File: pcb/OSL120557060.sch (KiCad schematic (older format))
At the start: 75 parts, among them J1 USB_B_Micro, J2 USB_B_Micro, J3 AVR-ISP-6, SW1 SW_SPST, SW10 SW_SPST, SW11 SW_SPST, SW12 SW_SPST, SW13 SW_SPST, SW14 SW_SPST, SW15 SW_SPST, SW16 SW_SPST, SW17 SW_SPST, SW18 SW_SPST, SW19 SW_SPST, SW2 SW_SPST, SW20 SW_SPST, SW21 SW_SPST, SW22 SW_SPST, SW23 SW_SPST, SW24 SW_SPST, SW25 SW_SPST, SW26 SW_SPST, SW27 SW_SPST, SW28 SW_SPST, SW29 SW_SPST, SW3 SW_SPST, SW30 SW_SPST, SW4 SW_SPST, SW5 SW_SPST, SW6 SW_SPST, SW7 SW_SPST, SW8 SW_SPST, SW9 SW_SPST, U1 ATmega328-PU, X1 16MHz

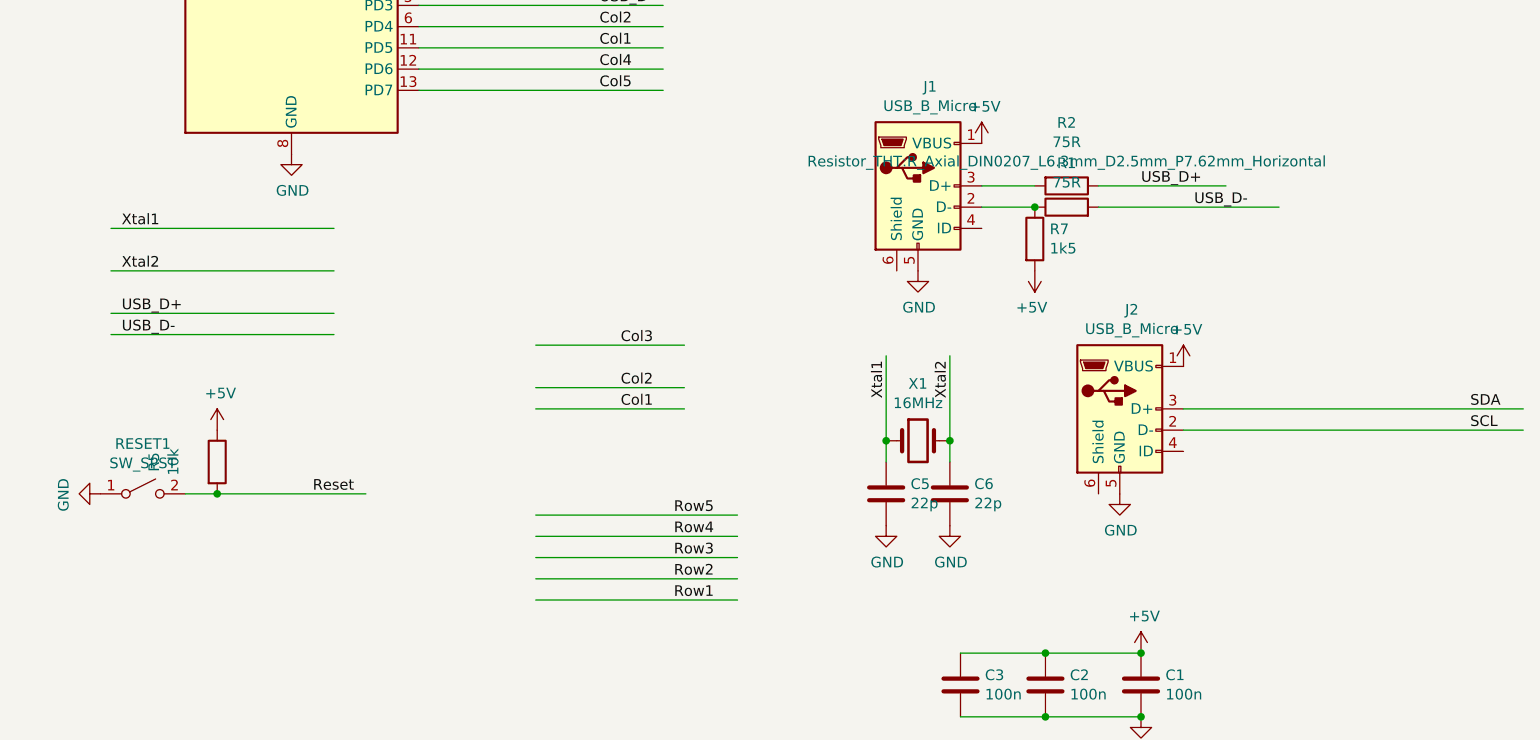
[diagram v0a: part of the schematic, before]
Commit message: updated schematic with reset switch
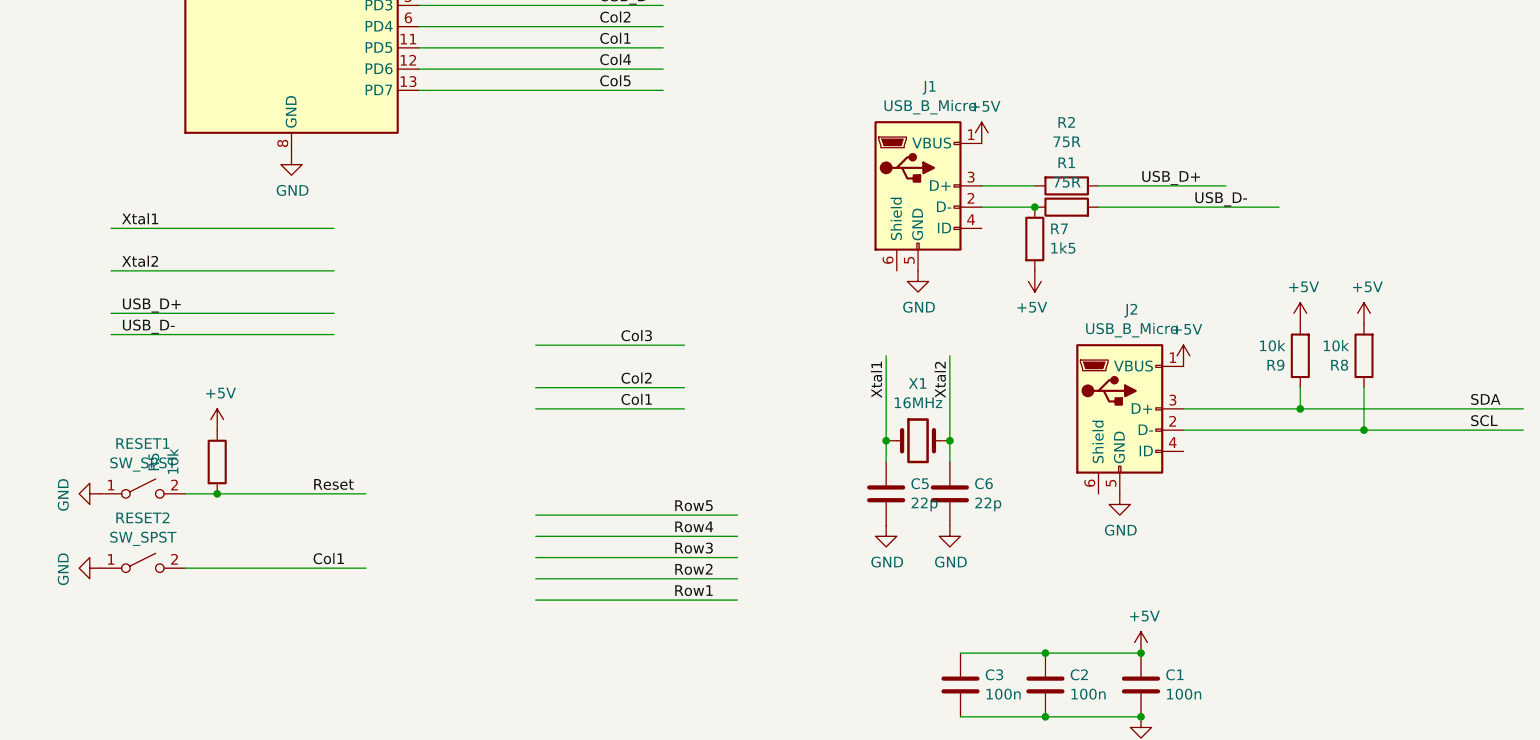
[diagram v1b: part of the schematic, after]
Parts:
- added R8, R9: 10k, Resistor_THT:R_Axial_DIN0204_L3.6mm_D1.6mm_P5.08mm_Horizontal, symbol Device:R
- added RESET2: SW_SPST, Button_Switch_THT:SW_PUSH_6mm_H4.3mm, symbol Switch:SW_SPST
- R1, R2, R5, R7: footprint Resistor_THT:R_Axial_DIN0207_L6.3mm_D2.5mm_P7.62mm_Horizontal -> Resistor_THT:R_Axial_DIN0204_L3.6mm_D1.6mm_P5.08mm_Horizontal
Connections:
- wire segments 125 -> 130
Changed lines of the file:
@@
 EESchema Schematic File Version 4
-LIBS:osl-12x5-57-cache
+LIBS:OSL120557060-cache
 EELAYER 29 0
 EELAYER END
@@
 F 0 "R2" V 5103 4700 50  0000 C CNN
 F 1 "75R" V 5194 4700 50  0000 C CNN
-F 2 "Resistor_THT:R_Axial_DIN0207_L6.3mm_D2.5mm_P7.62mm_Horizontal" V 5285 4700 50  0000 C CNN
+F 2 "Resistor_THT:R_Axial_DIN0204_L3.6mm_D1.6mm_P5.08mm_Horizontal" V 5285 4700 50  0001 C CNN
 F 3 "~" H 5400 4700 50  0001 C CNN
 	1    5400 4700
@@
 F 0 "R1" V 5607 4800 50  0000 C CNN
 F 1 "75R" V 5516 4800 50  0000 C CNN
-F 2 "Resistor_THT:R_Axial_DIN0207_L6.3mm_D2.5mm_P7.62mm_Horizontal" V 5330 4800 50  0001 C CNN
+F 2 "Resistor_THT:R_Axial_DIN0204_L3.6mm_D1.6mm_P5.08mm_Horizontal" V 5330 4800 50  0001 C CNN
 F 3 "~" H 5400 4800 50  0001 C CNN
 	1    5400 4800
@@
 F 0 "R5" V 1103 6000 50  0000 C CNN
 F 1 "10k" V 1194 6000 50  0000 C CNN
-F 2 "Resistor_THT:R_Axial_DIN0207_L6.3mm_D2.5mm_P7.62mm_Horizontal" V 1285 6000 50  0001 C CNN
+F 2 "Resistor_THT:R_Axial_DIN0204_L3.6mm_D1.6mm_P5.08mm_Horizontal" V 1285 6000 50  0001 C CNN
 F 3 "~" H 1400 6000 50  0001 C CNN
 	1    1400 6000
@@
 	6500 2500 6500 3000
 Wire Wire Line
-	5950 5750 7550 5750
+	5950 5750 6500 5750
 $Comp
 L MCU_Microchip_ATmega:ATmega328-PU U1
@@
 F 0 "R7" H 5320 4996 50  0000 L CNN
 F 1 "1k5" H 5320 4905 50  0000 L CNN
-F 2 "Resistor_THT:R_Axial_DIN0207_L6.3mm_D2.5mm_P7.62mm_Horizontal" V 5180 4950 50  0001 C CNN
+F 2 "Resistor_THT:R_Axial_DIN0204_L3.6mm_D1.6mm_P5.08mm_Horizontal" V 5180 4950 50  0001 C CNN
 F 3 "~" H 5250 4950 50  0001 C CNN
 	1    5250 4950
@@
 $EndComp
 Wire Wire Line
-	5950 5850 7550 5850
+	5950 5850 6800 5850
 Text Label 7300 5850 0    50   ~ 0
 SCL
@@
 	1    0    0    -1
 $EndComp
+$Comp
+L Device:R R9
+U 1 1 5D0C0A85
+P 6500 5500
+F 0 "R9" H 6570 5546 50  0000 L CNN
+F 1 "10k" H 6570 5455 50  0000 L CNN
+F 2 "Resistor_THT:R_Axial_DIN0204_L3.6mm_D1.6mm_P5.08mm_Horizontal" V 6430 5500 50  0001 C CNN
+F 3 "~" H 6500 5500 50  0001 C CNN
+	1    6500 5500
+	-1   0    0    1
+$EndComp
+$Comp
+L power:+5V #PWR0117
+U 1 1 5D0C0A8B
+P 6500 5350
+F 0 "#PWR0117" H 6500 5200 50  0001 C CNN
+F 1 "+5V" H 6515 5523 50  0000 C CNN
+F 2 "" H 6500 5350 50  0001 C CNN
+F 3 "" H 6500 5350 50  0001 C CNN
+	1    6500 5350
+	1    0    0    -1
+$EndComp
+$Comp
+L Device:R R8
+U 1 1 5D0C6334
+P 6800 5500
+F 0 "R8" H 6870 5546 50  0000 L CNN
+F 1 "10k" H 6870 5455 50  0000 L CNN
+F 2 "Resistor_THT:R_Axial_DIN0204_L3.6mm_D1.6mm_P5.08mm_Horizontal" V 6730 5500 50  0001 C CNN
+F 3 "~" H 6800 5500 50  0001 C CNN
+	1    6800 5500
+	-1   0    0    1
+$EndComp
+$Comp
+L power:+5V #PWR0118
+U 1 1 5D0C633A
+P 6800 5350
+F 0 "#PWR0118" H 6800 5200 50  0001 C CNN
+F 1 "+5V" H 6815 5523 50  0000 C CNN
+F 2 "" H 6800 5350 50  0001 C CNN
+F 3 "" H 6800 5350 50  0001 C CNN
+	1    6800 5350
+	1    0    0    -1
+$EndComp
+Wire Wire Line
+	6800 5650 6800 5850
+Connection ~ 6800 5850
+Wire Wire Line
+	6800 5850 7550 5850
+Wire Wire Line
+	6500 5650 6500 5750
+Connection ~ 6500 5750
+Wire Wire Line
+	6500 5750 7550 5750
+$Comp
+L Switch:SW_SPST RESET2
+U 1 1 5D1219A3
+P 1050 6500
+F 0 "RESET2" H 1050 6735 50  0000 C CNN
+F 1 "SW_SPST" H 1050 6644 50  0000 C CNN
+F 2 "Button_Switch_THT:SW_PUSH_6mm_H4.3mm" H 1050 6500 50  0001 C CNN
+F 3 "~" H 1050 6500 50  0001 C CNN
+	1    1050 6500
+	1    0    0    -1
+$EndComp
+$Comp
+L power:GND #PWR0119
+U 1 1 5D128184
+P 850 6500
+F 0 "#PWR0119" H 850 6250 50  0001 C CNN
+F 1 "GND" H 855 6327 50  0000 C CNN
+F 2 "" H 850 6500 50  0001 C CNN
+F 3 "" H 850 6500 50  0001 C CNN
+	1    850  6500
+	0    1    1    0
+$EndComp
+Wire Wire Line
+	1250 6500 2100 6500
+Text Label 1850 6500 0    50   ~ 0
+Col1
 $EndSCHEMATC

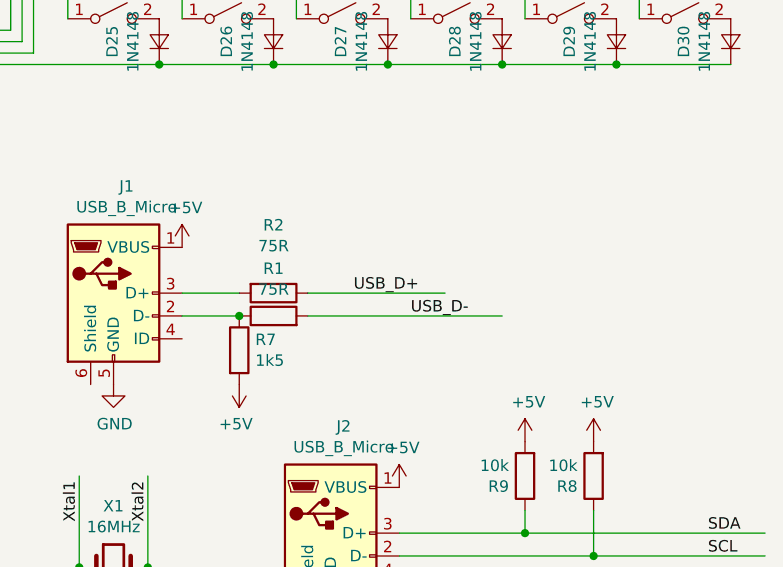
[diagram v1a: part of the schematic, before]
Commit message: added smaller reset switches moved components to allow for all around plate
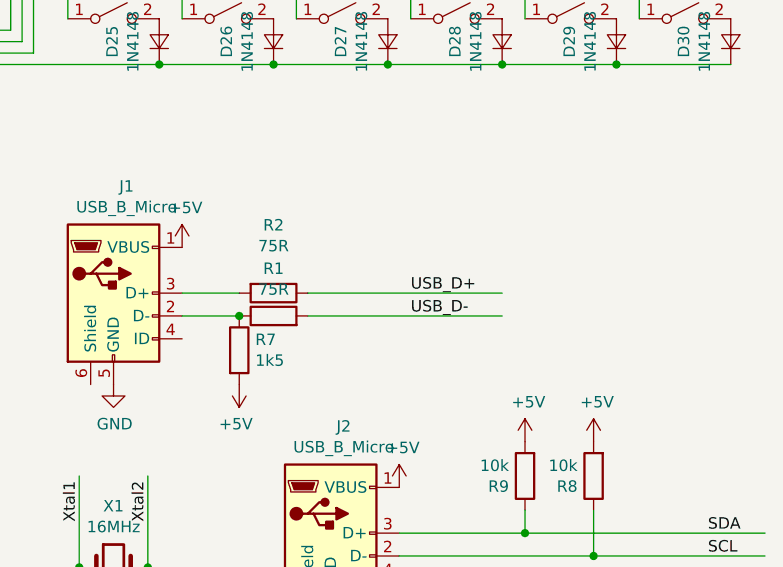
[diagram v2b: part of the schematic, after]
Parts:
- C1, C2, C3, C5, C6: footprint Capacitor_THT:C_Rect_L4.0mm_W2.5mm_P2.50mm -> Capacitor_THT:C_Disc_D3.0mm_W1.6mm_P2.50mm
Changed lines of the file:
@@
 F 0 "C6" H 4965 6196 50  0000 L CNN
 F 1 "22p" H 4965 6105 50  0000 L CNN
-F 2 "Capacitor_THT:C_Rect_L4.0mm_W2.5mm_P2.50mm" H 4888 6000 50  0001 C CNN
+F 2 "Capacitor_THT:C_Disc_D3.0mm_W1.6mm_P2.50mm" H 4888 6000 50  0001 C CNN
 F 3 "~" H 4850 6150 50  0001 C CNN
 	1    4850 6150
@@
 F 0 "C5" H 4435 6196 50  0000 R CNN
 F 1 "22p" H 4435 6105 50  0000 R CNN
-F 2 "Capacitor_THT:C_Rect_L4.0mm_W2.5mm_P2.50mm" H 4588 6000 50  0001 C CNN
+F 2 "Capacitor_THT:C_Disc_D3.0mm_W1.6mm_P2.50mm" H 4588 6000 50  0001 C CNN
 F 3 "~" H 4550 6150 50  0001 C CNN
 	1    4550 6150
@@
 	5000 4700 5250 4700
 Wire Wire Line
-	5550 4700 6150 4700
-Wire Wire Line
 	5550 4800 6400 4800
-Text Label 5750 4700 0    50   ~ 0
+Text Label 6000 4700 0    50   ~ 0
 USB_D+
 Text Label 6000 4800 0    50   ~ 0
@@
 F 0 "C1" H 5865 7096 50  0000 L CNN
 F 1 "100n" H 5865 7005 50  0000 L CNN
-F 2 "Capacitor_THT:C_Rect_L4.0mm_W2.5mm_P2.50mm" H 5788 6900 50  0001 C CNN
+F 2 "Capacitor_THT:C_Disc_D3.0mm_W1.6mm_P2.50mm" H 5788 6900 50  0001 C CNN
 F 3 "~" H 5750 7050 50  0001 C CNN
 	1    5750 7050
@@
 F 0 "C2" H 5415 7096 50  0000 L CNN
 F 1 "100n" H 5415 7005 50  0000 L CNN
-F 2 "Capacitor_THT:C_Rect_L4.0mm_W2.5mm_P2.50mm" H 5338 6900 50  0001 C CNN
+F 2 "Capacitor_THT:C_Disc_D3.0mm_W1.6mm_P2.50mm" H 5338 6900 50  0001 C CNN
 F 3 "~" H 5300 7050 50  0001 C CNN
 	1    5300 7050
@@
 F 0 "C3" H 5015 7096 50  0000 L CNN
 F 1 "100n" H 5015 7005 50  0000 L CNN
-F 2 "Capacitor_THT:C_Rect_L4.0mm_W2.5mm_P2.50mm" H 4938 6900 50  0001 C CNN
+F 2 "Capacitor_THT:C_Disc_D3.0mm_W1.6mm_P2.50mm" H 4938 6900 50  0001 C CNN
 F 3 "~" H 4900 7050 50  0001 C CNN
 	1    4900 7050
@@
 Text Label 1850 6500 0    50   ~ 0
 Col1
+Wire Wire Line
+	5550 4700 6400 4700
 $EndSCHEMATC

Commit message: changed component footprints
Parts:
- R1, R2, R5, R7, R8, R9: footprint Resistor_THT:R_Axial_DIN0204_L3.6mm_D1.6mm_P5.08mm_Horizontal -> Resistor_THT:R_Axial_DIN0207_L6.3mm_D2.5mm_P7.62mm_Horizontal
- RESET1, RESET2: footprint Button_Switch_THT:SW_PUSH_6mm_H4.3mm -> Button_Switch_SMD:SW_SPST_B3U-1000P
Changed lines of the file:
@@
 F 0 "R2" V 5103 4700 50  0000 C CNN
 F 1 "75R" V 5194 4700 50  0000 C CNN
-F 2 "Resistor_THT:R_Axial_DIN0204_L3.6mm_D1.6mm_P5.08mm_Horizontal" V 5285 4700 50  0001 C CNN
+F 2 "Resistor_THT:R_Axial_DIN0207_L6.3mm_D2.5mm_P7.62mm_Horizontal" V 5285 4700 50  0001 C CNN
 F 3 "~" H 5400 4700 50  0001 C CNN
 	1    5400 4700
@@
 F 0 "R1" V 5607 4800 50  0000 C CNN
 F 1 "75R" V 5516 4800 50  0000 C CNN
-F 2 "Resistor_THT:R_Axial_DIN0204_L3.6mm_D1.6mm_P5.08mm_Horizontal" V 5330 4800 50  0001 C CNN
+F 2 "Resistor_THT:R_Axial_DIN0207_L6.3mm_D2.5mm_P7.62mm_Horizontal" V 5330 4800 50  0001 C CNN
 F 3 "~" H 5400 4800 50  0001 C CNN
 	1    5400 4800
@@
 F 0 "RESET1" H 1050 6385 50  0000 C CNN
 F 1 "SW_SPST" H 1050 6294 50  0000 C CNN
-F 2 "Button_Switch_THT:SW_PUSH_6mm_H4.3mm" H 1050 6150 50  0001 C CNN
+F 2 "Button_Switch_SMD:SW_SPST_B3U-1000P" H 1050 6150 50  0001 C CNN
 F 3 "~" H 1050 6150 50  0001 C CNN
 	1    1050 6150
@@
 F 0 "R5" V 1103 6000 50  0000 C CNN
 F 1 "10k" V 1194 6000 50  0000 C CNN
-F 2 "Resistor_THT:R_Axial_DIN0204_L3.6mm_D1.6mm_P5.08mm_Horizontal" V 1285 6000 50  0001 C CNN
+F 2 "Resistor_THT:R_Axial_DIN0207_L6.3mm_D2.5mm_P7.62mm_Horizontal" V 1285 6000 50  0001 C CNN
 F 3 "~" H 1400 6000 50  0001 C CNN
 	1    1400 6000
@@
 F 0 "R7" H 5320 4996 50  0000 L CNN
 F 1 "1k5" H 5320 4905 50  0000 L CNN
-F 2 "Resistor_THT:R_Axial_DIN0204_L3.6mm_D1.6mm_P5.08mm_Horizontal" V 5180 4950 50  0001 C CNN
+F 2 "Resistor_THT:R_Axial_DIN0207_L6.3mm_D2.5mm_P7.62mm_Horizontal" V 5180 4950 50  0001 C CNN
 F 3 "~" H 5250 4950 50  0001 C CNN
 	1    5250 4950
@@
 F 0 "R9" H 6570 5546 50  0000 L CNN
 F 1 "10k" H 6570 5455 50  0000 L CNN
-F 2 "Resistor_THT:R_Axial_DIN0204_L3.6mm_D1.6mm_P5.08mm_Horizontal" V 6430 5500 50  0001 C CNN
+F 2 "Resistor_THT:R_Axial_DIN0207_L6.3mm_D2.5mm_P7.62mm_Horizontal" V 6430 5500 50  0001 C CNN
 F 3 "~" H 6500 5500 50  0001 C CNN
 	1    6500 5500
@@
 F 0 "R8" H 6870 5546 50  0000 L CNN
 F 1 "10k" H 6870 5455 50  0000 L CNN
-F 2 "Resistor_THT:R_Axial_DIN0204_L3.6mm_D1.6mm_P5.08mm_Horizontal" V 6730 5500 50  0001 C CNN
+F 2 "Resistor_THT:R_Axial_DIN0207_L6.3mm_D2.5mm_P7.62mm_Horizontal" V 6730 5500 50  0001 C CNN
 F 3 "~" H 6800 5500 50  0001 C CNN
 	1    6800 5500
@@
 F 0 "RESET2" H 1050 6735 50  0000 C CNN
 F 1 "SW_SPST" H 1050 6644 50  0000 C CNN
-F 2 "Button_Switch_THT:SW_PUSH_6mm_H4.3mm" H 1050 6500 50  0001 C CNN
+F 2 "Button_Switch_SMD:SW_SPST_B3U-1000P" H 1050 6500 50  0001 C CNN
 F 3 "~" H 1050 6500 50  0001 C CNN
 	1    1050 6500
